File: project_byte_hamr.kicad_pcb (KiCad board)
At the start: 4 copper layers, 125.5 x 80.3 mm, 93 parts, among them J3 Bus_Apple_II_Card_Side, J4 CONN_02X03, U1 LFE5U-25F-6BG381C, U10 IS25LP128F-JBLE, U11 SN74LVC8T245, U12 SN74LVC8T245, U13 SN74LVC8T245, U14 SN74LVC8T245, U2 MT48LC16M16A2TG, U3 TLV62569DBV, U4 TLV62569DBV, U5 TLV62569DBV, U6 FT231XQ, U8 SN74LVC8T245, U9 SN74LVC8T245, Y1 FNETHE025

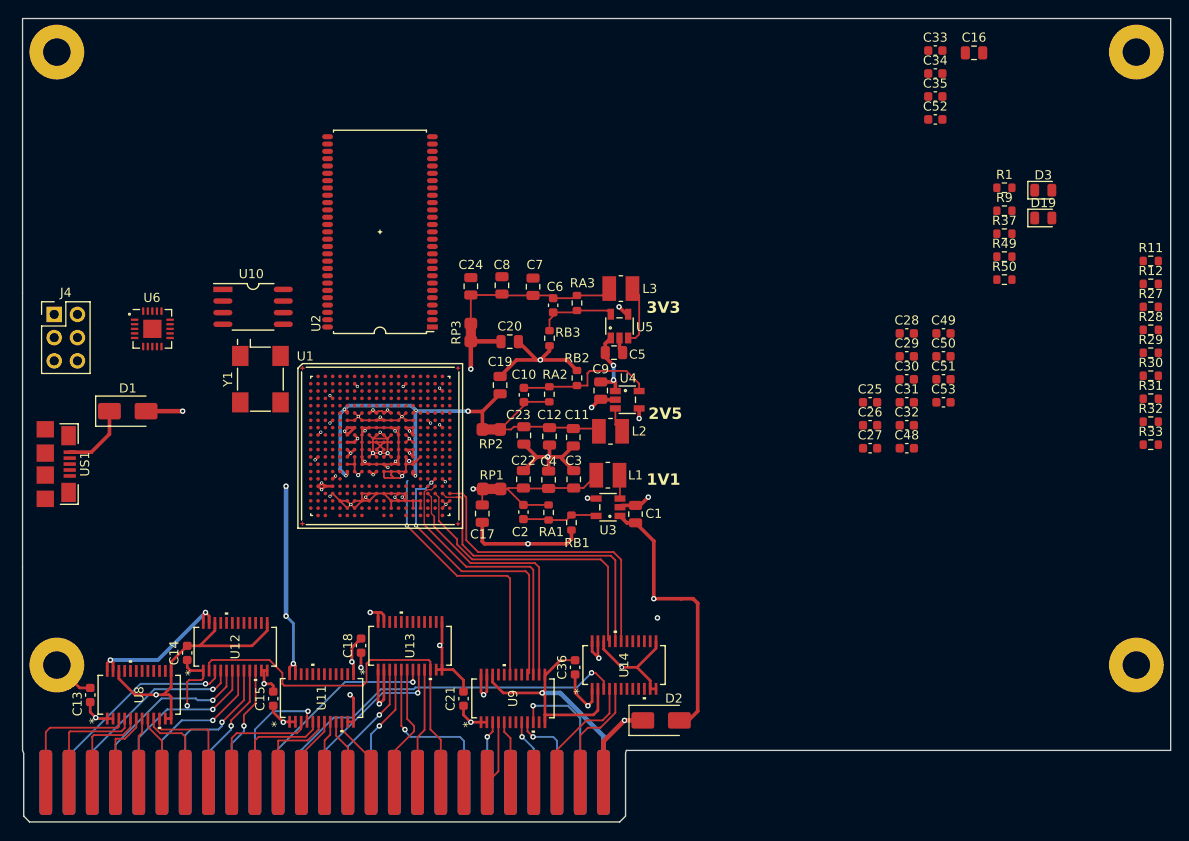
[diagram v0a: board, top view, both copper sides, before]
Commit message: Moved routing to right side of FPGA
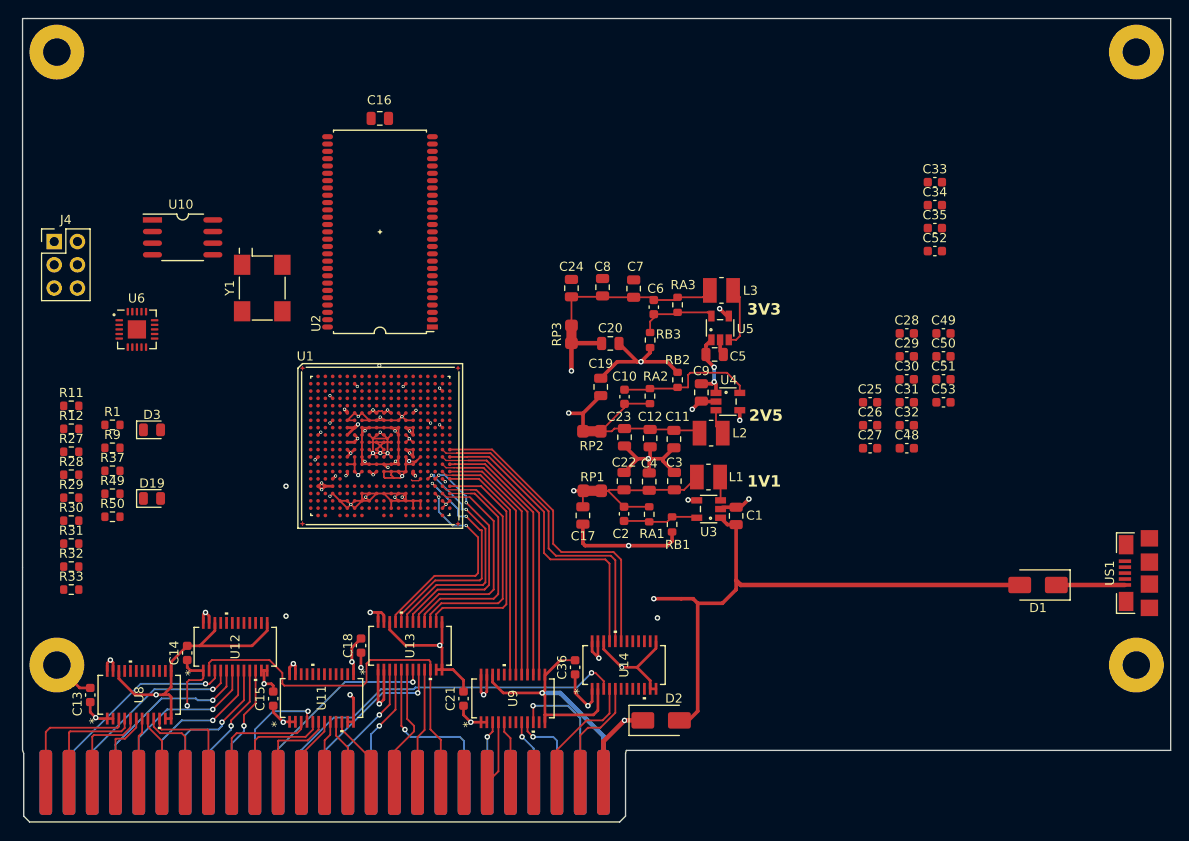
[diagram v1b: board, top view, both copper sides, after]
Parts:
- moved US1 121.3 mm to (173.2, 110.7), turned to 90 degrees
- moved R11 119.1 mm to (55.3, 92.4)
- moved R12 119.1 mm to (55.3, 94.9)
- moved R27 119.1 mm to (55.3, 97.4)
- moved R28 119.1 mm to (55.3, 100.0)
- moved R29 119.1 mm to (55.3, 102.5)
- moved R30 119.1 mm to (55.3, 105.0)
- moved R31 119.1 mm to (55.3, 107.5)
- moved R32 119.1 mm to (55.3, 110.0)
- moved R33 119.1 mm to (55.3, 112.5)
- moved D19 102.1 mm to (64.2, 102.5)
- moved D1 101.3 mm to (161.0, 112.0), turned to 180 degrees
- moved R1 100.9 mm to (59.8, 94.5)
- moved R37 100.9 mm to (59.8, 99.5)
- moved R49 100.9 mm to (59.8, 102.0)
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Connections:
- U1 pad A4: ~{I/O_STROBE}_3V3 -> unconnected-(U1F-PL11A-PadA4)
- U1 pad G5: A15_3V3 -> unconnected-(U1F-PL41B-PadG5)
- U1 pad H1: Q3_3V3 -> unconnected-(U1E-PL53C-PadH1)
- U1 pad H3: A14_3V3 -> unconnected-(U1F-PL41D-PadH3)
- U1 pad K2: 7M_3V3 -> unconnected-(U1E-PL53A-PadK2)
- U1 pad L1: ~{INH}_3V3 -> unconnected-(U1E-PL65C-PadL1)
- U1 pad L19: unconnected-(U1D-PCLKT3_0-PadL19) -> INT_OUT_3V3
- U1 pad L20: unconnected-(U1D-PCLKT3_1-PadL20) -> DMA_OUT_3V3
- U1 pad L4: ~{RES}_3V3 -> unconnected-(U1E-PL56C-PadL4)
- U1 pad M1: PHI1_3V3 -> unconnected-(U1E-PL89B-PadM1)
- U1 pad M19: unconnected-(U1D-PCLKC3_0-PadM19) -> DMA_IN_3V3
- U1 pad M20: unconnected-(U1D-PCLKC3_1-PadM20) -> USER1_3V3
- U1 pad M3: R/~{W}_3V3 -> unconnected-(U1E-PL86B-PadM3)
- U1 pad N1: PHI0_3V3 -> unconnected-(U1E-PL89D-PadN1)
- U1 pad N19: unconnected-(U1D-PR83A-PadN19) -> ~{NMI}_3V3
- U1 pad N20: unconnected-(U1D-PR83B-PadN20) -> INT_IN_3V3
- U1 pad P19: unconnected-(U1D-PR83C-PadP19) -> ~{I/O_STROBE}_3V3
- U1 pad P20: unconnected-(U1D-PR86A-PadP20) -> RDY_3V3
- U1 pad R16: RDY_3V3 -> unconnected-(U1D-PR56C-PadR16)
- U1 pad R17: unconnected-(U1D-PR56D-PadR17) -> ~{INH}_3V3
- U1 pad R18: ~{NMI}_3V3 -> A14_3V3
- U1 pad R20: unconnected-(U1D-PR86B-PadR20) -> ~{RES}_3V3
- U1 pad T18: INT_IN_3V3 -> 7M_3V3
- U1 pad T19: unconnected-(U1D-PR89A-PadT19) -> A15_3V3
- U1 pad T20: unconnected-(U1D-PR86C-PadT20) -> R/~{W}_3V3
- U1 pad U17: DMA_IN_3V3 -> unconnected-(U1D-PR92B-PadU17)
- U1 pad U18: USER1_3V3 -> Q3_3V3
- U1 pad U19: INT_OUT_3V3 -> PHI0_3V3
- U1 pad U20: DMA_OUT_3V3 -> PHI1_3V3
- U9 pad 17: unconnected-(U9-B5-Pad17) -> RDY_3V3
- U9 pad 18: unconnected-(U9-B4-Pad18) -> ~{I/O_STROBE}_3V3
- U9 pad 19: RDY_3V3 -> ~{RES}_3V3
- U9 pad 20: ~{I/O_STROBE}_3V3 -> unconnected-(U9-B2-Pad20)
- U9 pad 21: ~{RES}_3V3 -> unconnected-(U9-B1-Pad21)
- U9 pad 3: ~{RES}_5V -> unconnected-(U9-A1-Pad3)
- U9 pad 4: ~{I/O_STROBE}_5V -> unconnected-(U9-A2-Pad4)
- U9 pad 5: RDY_5V -> ~{RES}_5V
- U9 pad 6: unconnected-(U9-A4-Pad6) -> ~{I/O_STROBE}_5V
- U9 pad 7: unconnected-(U9-A5-Pad7) -> RDY_5V
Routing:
- net +5V: track 45.7 -> 76.5 mm, vias 7 -> 6
- net ~{I/O_STROBE}_3V3: track 0.00 -> 27.7 mm
- net R/~{W}_3V3: track 0.00 -> 26.5 mm
- net A15_3V3: track 0.00 -> 26.4 mm
- net ~{INH}_3V3: track 0.00 -> 26.0 mm, vias 0 -> 2
- net ~{RES}_3V3: track 0.00 -> 26.0 mm
- net A14_3V3: track 0.00 -> 25.7 mm, vias 0 -> 2
- net 7M_3V3: track 0.00 -> 24.9 mm, vias 0 -> 2
- net PHI1_3V3: track 0.00 -> 24.6 mm
- net PHI0_3V3: track 0.00 -> 24.5 mm
- net Q3_3V3: track 0.00 -> 23.2 mm, vias 0 -> 2
- net +1V1: track 37.9 -> 49.0 mm
- net +2V5: track 37.2 -> 48.2 mm
- net GND: track 240.2 -> 248.4 mm
- net +3V3: track 113.3 -> 121.2 mm, vias 19 -> 20
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
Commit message: Routed Level Shifters + Flash
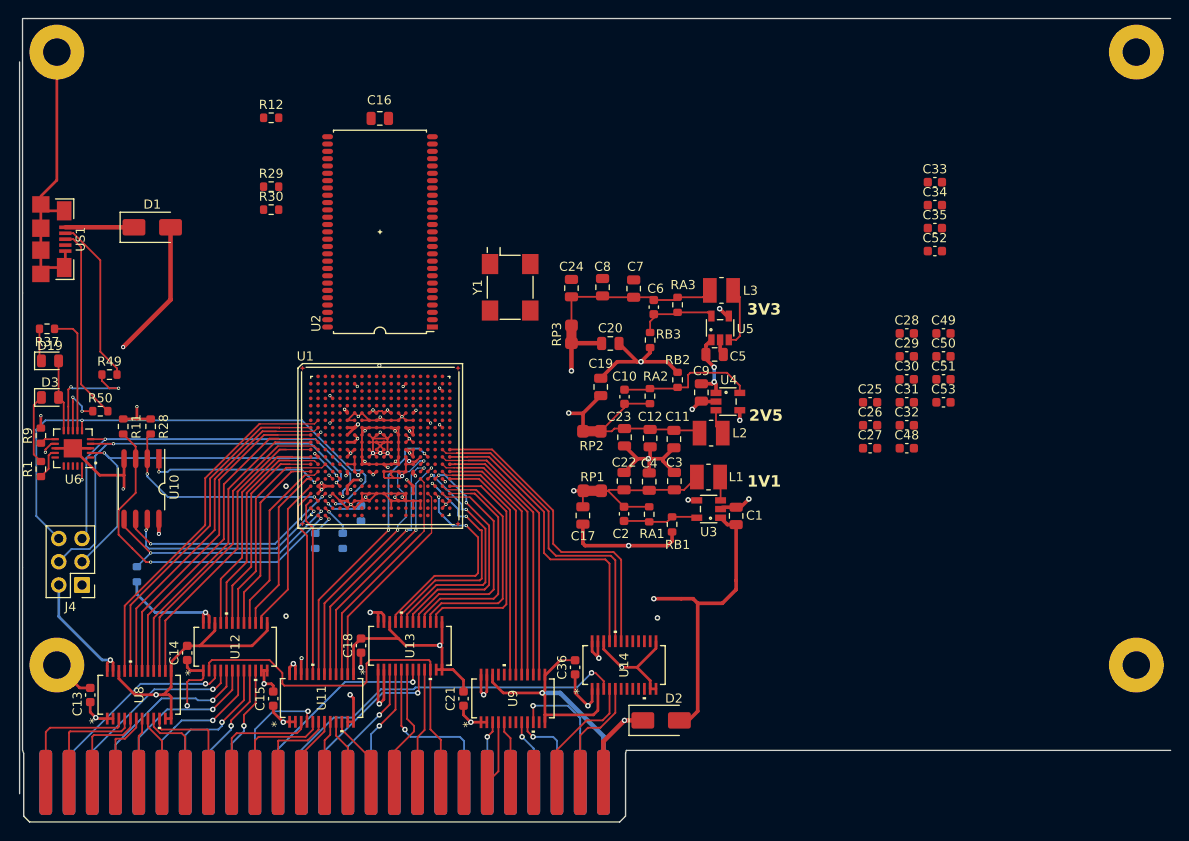
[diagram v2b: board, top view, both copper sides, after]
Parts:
- R27, R31, R32, R33: moved to B.Cu
- moved US1 126.6 mm to (52.0, 74.2), turned to -90 degrees
- moved D1 104.4 mm to (64.2, 72.9), turned to 0 degrees
- moved R12 40.4 mm to (77.2, 60.9)
- moved R29 40.4 mm to (77.2, 68.5)
- moved R30 40.4 mm to (77.2, 71.0)
- moved J4 37.7 mm to (56.5, 112.0), turned to 180 degrees
- moved R33 32.8 mm to (87.0, 104.2), turned to 90 degrees
- moved R31 29.7 mm to (85.0, 107.2), turned to 90 degrees
- moved U10 27.9 mm to (63.0, 101.5), turned to -90 degrees
- moved Y1 27.1 mm to (103.3, 79.5)
- moved R32 26.8 mm to (82.0, 107.2), turned to 90 degrees
- moved D19 18.7 mm to (53.0, 87.5)
- moved R37 17.1 mm to (52.7, 84.0), turned to 180 degrees
- moved R27 15.2 mm to (62.5, 110.8), turned to 90 degrees
- moved U6 14.8 mm to (55.5, 97.1), turned to 180 degrees
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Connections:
- U1 pad A3: A0_3V3 -> unconnected-(U1F-PL14C-PadA3)
- U1 pad A5: A3_3V3 -> unconnected-(U1F-PL11B-PadA5)
- U1 pad B1: A11_3V3 -> unconnected-(U1F-PL35B-PadB1)
- U1 pad B18: unconnected-(U1B-PT116B-PadB18) -> SDRAM_A3
- U1 pad B20: SDRAM_A3 -> CLK_25MHz
- U1 pad B3: A4_3V3 -> unconnected-(U1F-PL14D-PadB3)
- U1 pad B4: A5_3V3 -> unconnected-(U1F-PL14B-PadB4)
- U1 pad B5: ~{I/O_SELECT}_3V3 -> unconnected-(U1F-PL11C-PadB5)
- U1 pad C2: A10_3V3 -> unconnected-(U1F-PL35D-PadC2)
- U1 pad C4: A1_3V3 -> unconnected-(U1F-PL14A-PadC4)
- U1 pad C5: A2_3V3 -> unconnected-(U1F-PL11D-PadC5)
- U1 pad D1: A13_3V3 -> unconnected-(U1F-PL38B-PadD1)
- U1 pad D3: A6_3V3 -> unconnected-(U1F-PL17D-PadD3)
- U1 pad D5: A7_3V3 -> unconnected-(U1F-PL17B-PadD5)
- U1 pad E1: A12_3V3 -> unconnected-(U1F-PL38D-PadE1)
- U1 pad E3: A9_3V3 -> unconnected-(U1F-PL20B-PadE3)
- U1 pad F5: A8_3V3 -> unconnected-(U1F-PL20D-PadF5)
- U1 pad G2: CLK_25MHz -> ~{I/O_SELECT}_3V3
- U1 pad H1: unconnected-(U1E-PL53C-PadH1) -> A0_3V3
- U1 pad H2: unconnected-(U1E-PCLKT6_0-PadH2) -> A1_3V3
- U1 pad J1: D3_3V3 -> A2_3V3
- U1 pad J5: D1_3V3 -> unconnected-(U1E-PL50B-PadJ5)
- U1 pad K1: D2_3V3 -> A4_3V3
- U1 pad K2: unconnected-(U1E-PL53A-PadK2) -> A3_3V3
- U1 pad K3: D0_3V3 -> unconnected-(U1E-PL50D-PadK3)
- U1 pad L1: unconnected-(U1E-PL65C-PadL1) -> A6_3V3
- U1 pad L2: D7_3V3 -> A5_3V3
- U1 pad L5: D4_3V3 -> unconnected-(U1E-PL56D-PadL5)
- U1 pad M1: unconnected-(U1E-PL89B-PadM1) -> D0_3V3
- U1 pad M17: unconnected-(U1D-PR53B-PadM17) -> A8_3V3
- U1 pad N1: unconnected-(U1E-PL89D-PadN1) -> D2_3V3
- U1 pad N16: unconnected-(U1D-PR53A-PadN16) -> A9_3V3
- U1 pad N2: unconnected-(U1E-PL65A-PadN2) -> D1_3V3
- U1 pad N3: unconnected-(U1E-PL86A-PadN3) -> D3_3V3
- U1 pad N4: ~{DEVICE_SELECT}_3V3 -> unconnected-(U1E-PL83C-PadN4)
- U1 pad N5: D6_3V3 -> unconnected-(U1E-PL83B-PadN5)
- U1 pad P1: unconnected-(U1E-PL92A-PadP1) -> D4_3V3
- U1 pad P16: unconnected-(U1D-VREF1_3-PadP16) -> A10_3V3
- U1 pad P17: unconnected-(U1D-PR53D-PadP17) -> A11_3V3
- U1 pad P2: unconnected-(U1E-PL92B-PadP2) -> D5_3V3
- U1 pad P5: D5_3V3 -> unconnected-(U1E-PL83D-PadP5)
- U1 pad R1: unconnected-(U1G-D7-PadR1) -> D6_3V3
- U1 pad R16: unconnected-(U1D-PR56C-PadR16) -> A12_3V3
- U1 pad T1: unconnected-(U1G-D6-PadT1) -> D7_3V3
- U1 pad T10: (no net) -> unconnected-(U1H-VCCHTX0_D0CH1-PadT10)
- U1 pad T11: (no net) -> unconnected-(U1H-VCCHTX0_D1CH0-PadT11)
- U1 pad T12: (no net) -> unconnected-(U1H-VCCHRX0_D1CH0-PadT12)
- U1 pad T13: (no net) -> unconnected-(U1H-VCCHRX0_D1CH1-PadT13)
- U1 pad T14: (no net) -> unconnected-(U1H-VCCHTX0_D1CH1-PadT14)
- U1 pad T15: (no net) -> +1V1
- U1 pad T6: (no net) -> +1V1
- U1 pad T7: (no net) -> unconnected-(U1H-VCCHTX0_D0CH0-PadT7)
- U1 pad T8: (no net) -> unconnected-(U1H-VCCHRX0_D0CH0-PadT8)
- U1 pad T9: (no net) -> unconnected-(U1H-VCCHRX0_D0CH1-PadT9)
- U1 pad U1: unconnected-(U1G-D5/MISO2-PadU1) -> A7_3V3
- U1 pad U15: (no net) -> +1V1
- U1 pad U17: unconnected-(U1D-PR92B-PadU17) -> A13_3V3
- U1 pad U6: (no net) -> +1V1
- U1 pad V1: unconnected-(U1G-D4/MOSI2-PadV1) -> ~{DEVICE_SELECT}_3V3
- U1 pad V10: (no net) -> unconnected-(U1H-VCCAUXA0-PadV10)
- U1 pad V11: (no net) -> unconnected-(U1H-VCCAUXA0-PadV11)
- U1 pad V17: (no net) -> unconnected-(U1H-VCCAUXA1-PadV17)
- U1 pad V18: (no net) -> unconnected-(U1H-VCCAUXA1-PadV18)
- U1 pad W13: (no net) -> unconnected-(U1H-HDTXP0_D1CH0-PadW13)
- U1 pad W14: (no net) -> unconnected-(U1H-HDTXN0_D1CH0-PadW14)
- U1 pad W17: (no net) -> unconnected-(U1H-HDTXP0_D1CH1-PadW17)
- U1 pad W18: (no net) -> unconnected-(U1H-HDTXN0_D1CH1-PadW18)
- U1 pad W20: (no net) -> unconnected-(U1H-REFCLKN_D1-PadW20)
- U1 pad W4: (no net) -> unconnected-(U1H-HDTXP0_D0CH0-PadW4)
- U1 pad W5: (no net) -> unconnected-(U1H-HDTXN0_D0CH0-PadW5)
- U1 pad W8: (no net) -> unconnected-(U1H-HDTXP0_D0CH1-PadW8)
- U1 pad W9: (no net) -> unconnected-(U1H-HDTXN0_D0CH1-PadW9)
- U1 pad Y11: (no net) -> unconnected-(U1H-REFCLKP_D0-PadY11)
- U1 pad Y12: (no net) -> unconnected-(U1H-REFCLKN_D0-PadY12)
- U1 pad Y14: (no net) -> unconnected-(U1H-HDRXP0_D1CH0-PadY14)
- U1 pad Y15: (no net) -> unconnected-(U1H-HDRXN0_D1CH0-PadY15)
- U1 pad Y16: (no net) -> unconnected-(U1H-HDRXP0_D1CH1-PadY16)
- U1 pad Y17: (no net) -> unconnected-(U1H-HDRXN0_D1CH1-PadY17)
- U1 pad Y19: (no net) -> unconnected-(U1H-REFCLKP_D1-PadY19)
- U1 pad Y5: (no net) -> unconnected-(U1H-HDRXP0_D0CH0-PadY5)
- U1 pad Y6: (no net) -> unconnected-(U1H-HDRXN0_D0CH0-PadY6)
- U1 pad Y7: (no net) -> unconnected-(U1H-HDRXP0_D0CH1-PadY7)
- U1 pad Y8: (no net) -> unconnected-(U1H-HDRXN0_D0CH1-PadY8)
- U6 pad 12: USB5V -> +5V
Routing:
- net +3V3: track 121.2 -> 207.7 mm, vias 20 -> 25
- net GND: track 248.4 -> 314.5 mm, vias 41 -> 42
- net JTAG_TDO: track 0.00 -> 58.3 mm, vias 0 -> 2
- net JTAG_TCK: track 0.00 -> 47.4 mm, vias 0 -> 2
- net JTAG_TMS: track 0.00 -> 45.1 mm, vias 0 -> 2
- net JTAG_TDI: track 0.00 -> 42.5 mm, vias 0 -> 2
- net ~{I/O_SELECT}_3V3: track 0.00 -> 39.7 mm
- net A1_3V3: track 0.00 -> 38.2 mm
- net /flash/FLASH_nWP: track 0.00 -> 38.1 mm, vias 0 -> 2
- net A0_3V3: track 0.00 -> 37.9 mm
- net A2_3V3: track 0.00 -> 36.4 mm
- net A3_3V3: track 0.00 -> 36.4 mm
- net A5_3V3: track 0.00 -> 34.5 mm
- net A4_3V3: track 0.00 -> 34.4 mm
- net A6_3V3: track 0.00 -> 32.8 mm
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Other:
- board size 125.5 x 80.3 mm -> 125.8 x 84.7 mm

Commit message: Started SRAM routing
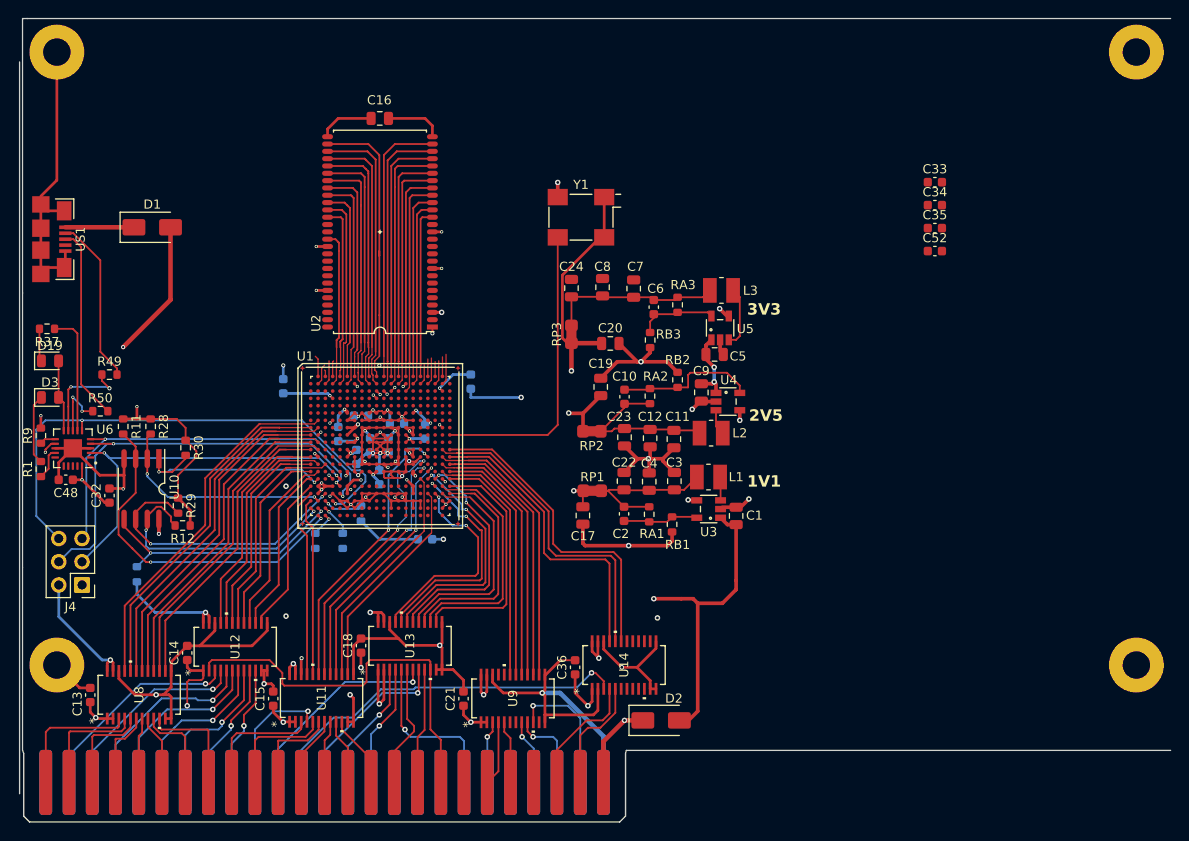
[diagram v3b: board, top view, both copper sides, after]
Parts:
- C25, C26, C27, C28, C29, C30, C31, C49, C50, C51, C53: moved to B.Cu
- moved C48 92.0 mm to (54.7, 100.5), turned to 180 degrees
- moved C32 87.5 mm to (59.5, 102.2), turned to 90 degrees
- moved C49 72.4 mm to (78.5, 90.3), turned to -90 degrees
- moved C29 62.7 mm to (84.5, 95.5), turned to -90 degrees
- moved C28 59.9 mm to (88.0, 96.7), turned to -90 degrees
- moved C53 59.8 mm to (90.9, 94.3)
- moved C31 59.7 mm to (87.0, 93.5), turned to 180 degrees
- moved C51 59.3 mm to (94.0, 107.0)
- moved C26 56.3 mm to (86.5, 98.0), turned to -90 degrees
- moved C25 54.3 mm to (89.0, 100.2), turned to 90 degrees
- moved C30 53.0 mm to (94.0, 95.2), turned to -90 degrees
- moved C27 52.6 mm to (90.0, 96.7), turned to -90 degrees
- moved C50 51.7 mm to (99.0, 89.8), turned to 90 degrees
- moved R12 45.6 mm to (67.5, 105.5), turned to 180 degrees
- moved R29 36.3 mm to (67.0, 103.3), turned to -90 degrees
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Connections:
- U1 pad A10: unconnected-(U1A-PCLKT0_1-PadA10) -> SDRAM_A4
- U1 pad A11: unconnected-(U1A-PCLKC0_1-PadA11) -> SDRAM_A3
- U1 pad A12: unconnected-(U1B-PT76A-PadA12) -> SDRAM_A1
- U1 pad A13: unconnected-(U1B-PT76B-PadA13) -> SDRAM_A10
- U1 pad A14: unconnected-(U1B-PT83A-PadA14) -> SDRAM_BA0
- U1 pad A15: unconnected-(U1B-PT103A-PadA15) -> SDRAM_nRAS
- U1 pad A16: SDRAM_A10 -> SDRAM_nWE
- U1 pad A17: SDRAM_nWE -> unconnected-(U1B-PT116A-PadA17)
- U1 pad A18: SDRAM_nCAS -> unconnected-(U1B-PT119A-PadA18)
- U1 pad A19: SDRAM_DQM0 -> unconnected-(U1B-PT121A-PadA19)
- U1 pad A5: unconnected-(U1F-PL11B-PadA5) -> SDRAM_DQM1
- U1 pad A6: unconnected-(U1A-PT4A-PadA6) -> SDRAM_CKE
- U1 pad A7: unconnected-(U1A-PT18A-PadA7) -> SDRAM_A11
- U1 pad A8: unconnected-(U1A-PT18B-PadA8) -> SDRAM_A8
- U1 pad A9: unconnected-(U1A-GR_PCLK0_1-PadA9) -> SDRAM_A6
- U1 pad B10: unconnected-(U1A-GR_PCLK0_0-PadB10) -> SDRAM_A5
- U1 pad B11: unconnected-(U1A-PCLKT0_0-PadB11) -> SDRAM_A2
- U1 pad B12: unconnected-(U1B-PCLKT1_0-PadB12) -> SDRAM_A0
- U1 pad B13: unconnected-(U1B-PT78A-PadB13) -> SDRAM_BA1
- U1 pad B15: unconnected-(U1B-PT105A-PadB15) -> SDRAM_nCAS
- U1 pad B16: SDRAM_nRAS -> unconnected-(U1B-PT110B-PadB16)
- U1 pad B17: SDRAM_nCS -> unconnected-(U1B-PT114A-PadB17)
- U1 pad B18: SDRAM_A3 -> unconnected-(U1B-PT116B-PadB18)
- U1 pad B20: CLK_25MHz -> unconnected-(U1B-PT121B-PadB20)
- U1 pad B3: unconnected-(U1F-PL14D-PadB3) -> SDRAM_DQM0
- U1 pad B4: unconnected-(U1F-PL14B-PadB4) -> SDRAM_D8
- U1 pad B5: unconnected-(U1F-PL11C-PadB5) -> SDRAM_CLK
- U1 pad B6: unconnected-(U1A-PT4B-PadB6) -> SDRAM_A12
- U1 pad B8: unconnected-(U1A-PT15B-PadB8) -> SDRAM_A9
- U1 pad B9: unconnected-(U1A-PT58A-PadB9) -> SDRAM_A7
- U1 pad C13: SDRAM_A0 -> unconnected-(U1B-PT78B-PadC13)
- U1 pad C14: unconnected-(U1B-PT83B-PadC14) -> SDRAM_nCS
- U1 pad C15: SDRAM_BA1 -> unconnected-(U1B-PT105B-PadC15)
- U1 pad C16: SDRAM_BA0 -> unconnected-(U1B-PT112A-PadC16)
- U1 pad D12: SDRAM_A2 -> unconnected-(U1B-GR_PCLK1_0-PadD12)
- U1 pad E13: SDRAM_A1 -> unconnected-(U1B-PT80B-PadE13)
- U1 pad E19: SDRAM_D8 -> unconnected-(U1C-PR35D-PadE19)
- U1 pad E20: SDRAM_DQM1 -> unconnected-(U1C-PR38A-PadE20)
- U1 pad F19: SDRAM_CLK -> unconnected-(U1C-PR38B-PadF19)
- U1 pad F20: SDRAM_CKE -> unconnected-(U1C-PR38C-PadF20)
- U1 pad G19: SDRAM_A12 -> unconnected-(U1C-GR_PCLK2_1-PadG19)
- U1 pad G20: SDRAM_A11 -> unconnected-(U1C-PR38D-PadG20)
- U1 pad H20: SDRAM_A9 -> unconnected-(U1C-PR41B-PadH20)
- U1 pad J19: SDRAM_A8 -> unconnected-(U1C-PCLKT2_1-PadJ19)
- U1 pad J20: SDRAM_A7 -> CLK_25MHz
- U1 pad K18: SDRAM_A6 -> unconnected-(U1C-PR41D-PadK18)
- U1 pad K19: SDRAM_A5 -> unconnected-(U1C-PCLKC2_1-PadK19)
- U1 pad K20: SDRAM_A4 -> unconnected-(U1C-PCLKC2_0-PadK20)
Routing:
- net +3V3: track 207.7 -> 324.6 mm, vias 25 -> 33
- net GND: track 314.5 -> 348.2 mm, vias 42 -> 44
- net CLK_25MHz: track 0.00 -> 32.8 mm
- net SDRAM_A4: track 0.00 -> 31.1 mm
- net SDRAM_A5: track 0.00 -> 30.5 mm
- net SDRAM_A3: track 0.00 -> 30.0 mm
- net SDRAM_A2: track 0.00 -> 29.9 mm
- net SDRAM_A6: track 0.00 -> 28.4 mm
- net SDRAM_A7: track 0.00 -> 28.2 mm
- net SDRAM_A0: track 0.00 -> 27.9 mm
- net SDRAM_A1: track 0.00 -> 27.8 mm
- net SDRAM_A8: track 0.00 -> 26.1 mm
- net SDRAM_A9: track 0.00 -> 26.0 mm
- net SDRAM_A10: track 0.00 -> 25.7 mm
- net SDRAM_BA1: track 0.00 -> 25.5 mm
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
